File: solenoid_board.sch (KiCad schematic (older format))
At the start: 34 parts, among them J2 MCU_LEFT_LEGS, J3 MCU_RIGHT_LEGS

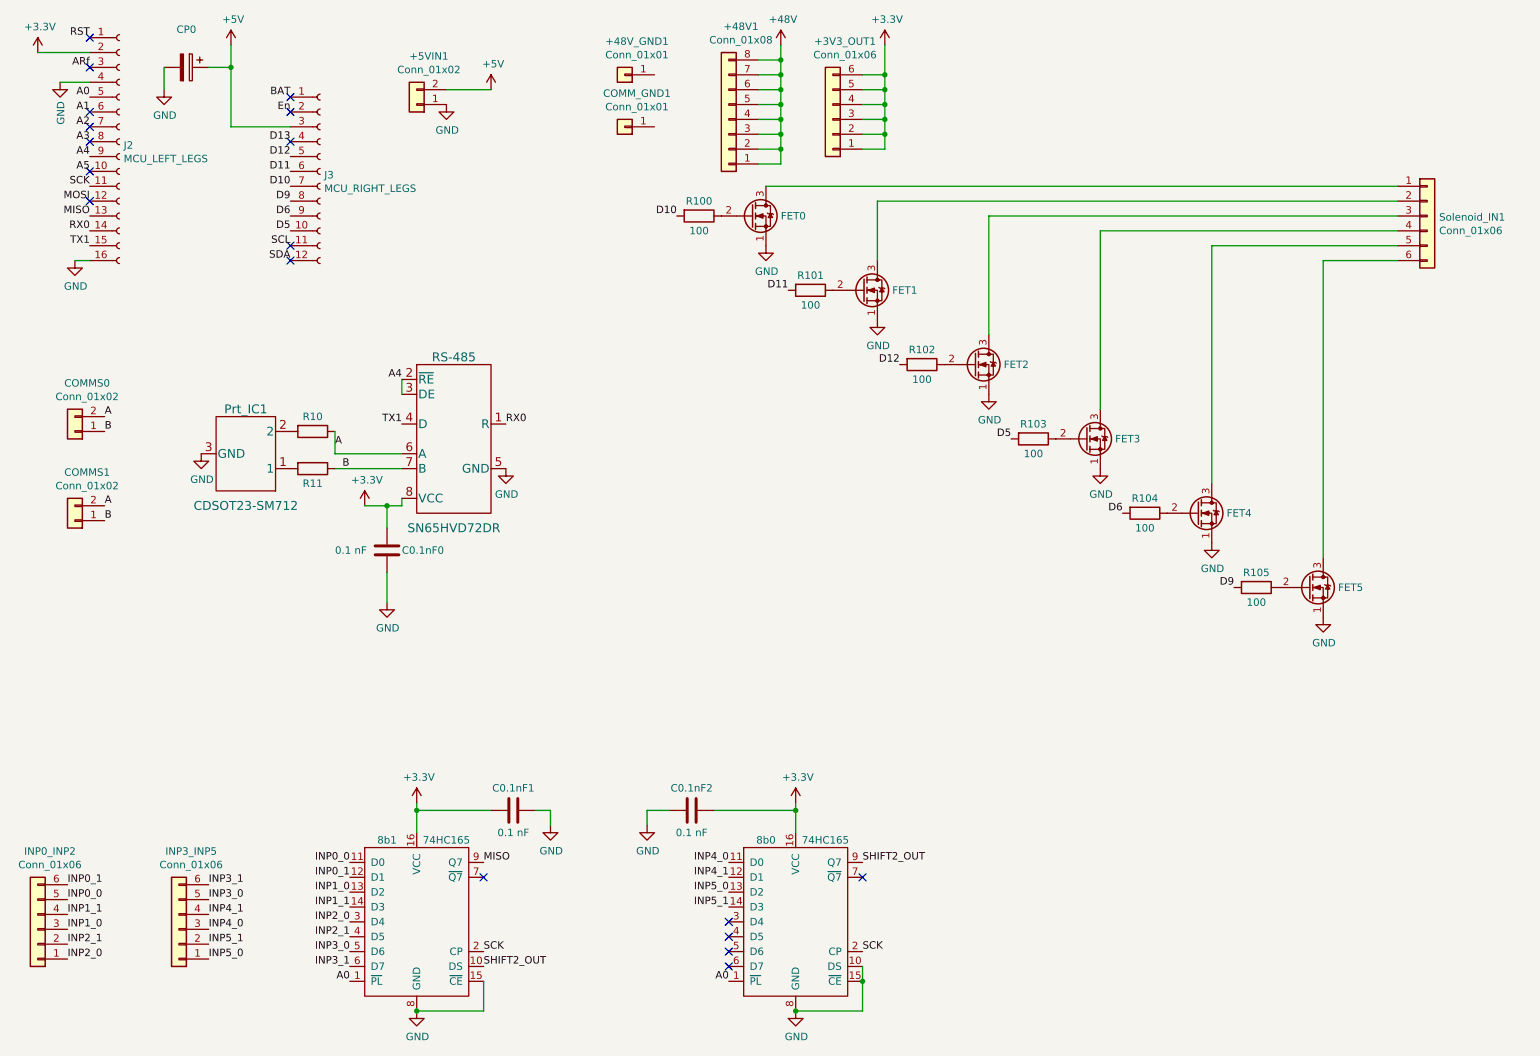
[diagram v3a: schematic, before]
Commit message: Changed pin labels around, re-routed MosFET area, need to route the 8-bit shifter and comms areas.
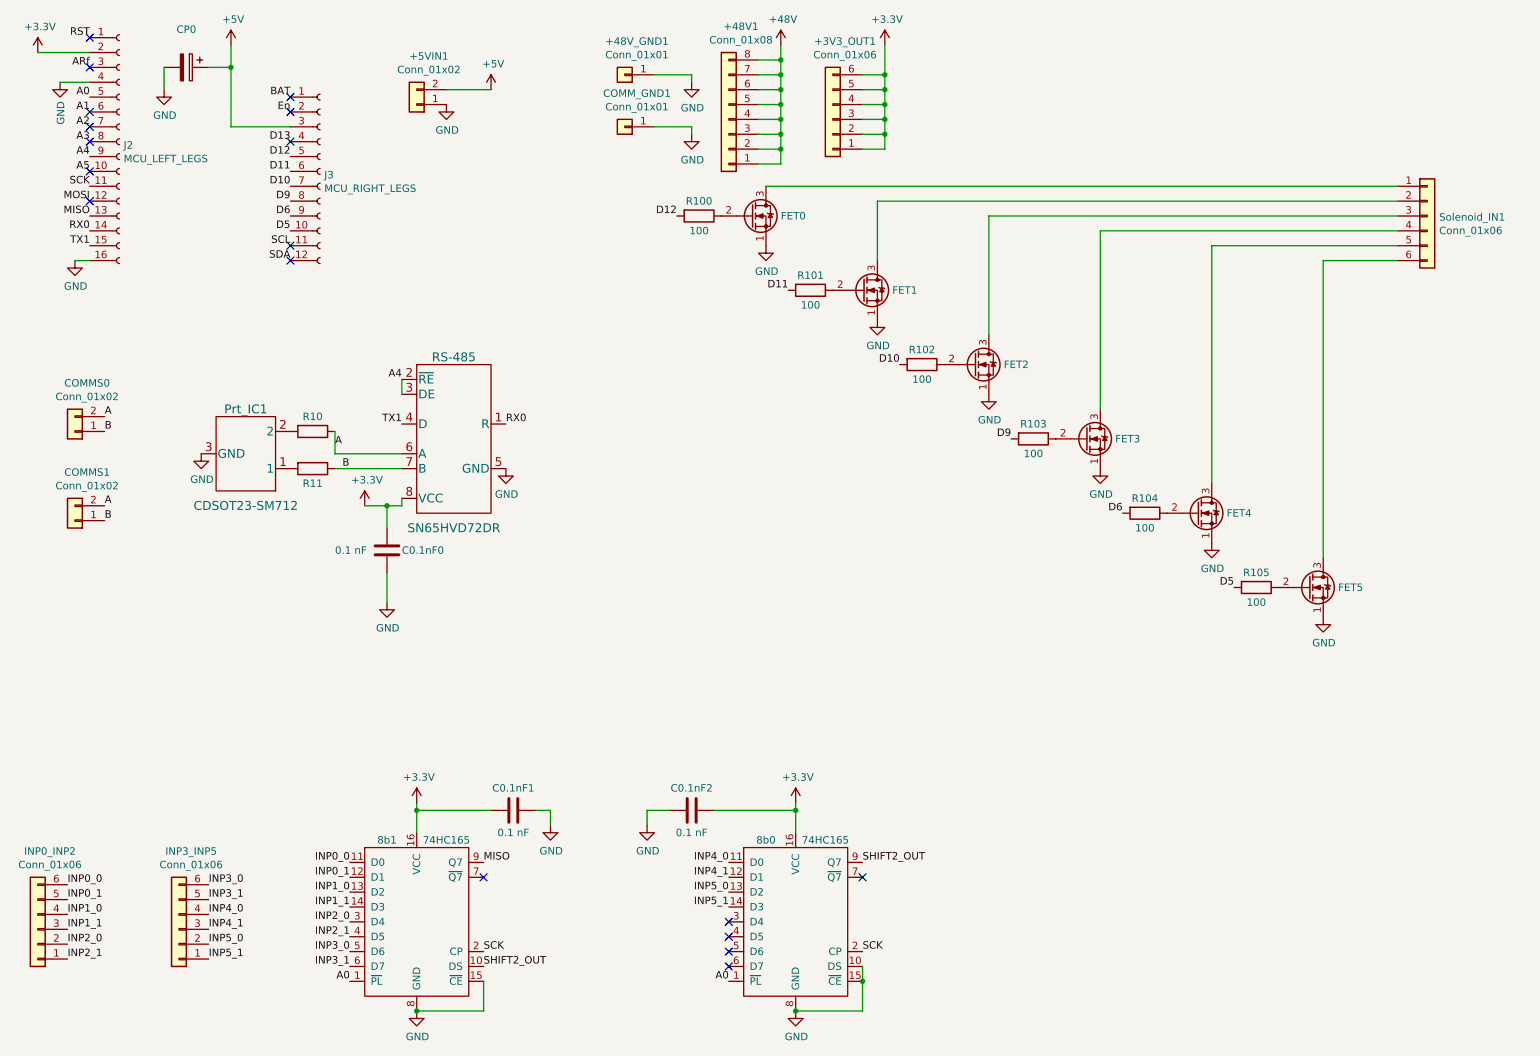
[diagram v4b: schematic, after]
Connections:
- net D10: now also R102.2; no longer R100.2
- net D12: now also R100.2; no longer R102.2
- net D5: now also R105.2; no longer R103.2
- net D9: now also R103.2; no longer R105.2
- net GND: now also +48V_GND1.1 (Pin_1), COMM_GND1.1 (Pin_1)
- net INP0_0: now also INP0_INP2.6 (Pin_6); no longer INP0_INP2.5 (Pin_5)
- net INP0_1: now also INP0_INP2.5 (Pin_5); no longer INP0_INP2.6 (Pin_6)
- net INP1_0: now also INP0_INP2.4 (Pin_4); no longer INP0_INP2.3 (Pin_3)
- net INP1_1: now also INP0_INP2.3 (Pin_3); no longer INP0_INP2.4 (Pin_4)
- net INP2_0: now also INP0_INP2.2 (Pin_2); no longer INP0_INP2.1 (Pin_1)
- net INP2_1: now also INP0_INP2.1 (Pin_1); no longer INP0_INP2.2 (Pin_2)
- net INP3_0: now also INP3_INP5.6 (Pin_6); no longer INP3_INP5.5 (Pin_5)
- net INP3_1: now also INP3_INP5.5 (Pin_5); no longer INP3_INP5.6 (Pin_6)
- net INP4_0: now also INP3_INP5.4 (Pin_4); no longer INP3_INP5.3 (Pin_3)
- net INP4_1: now also INP3_INP5.3 (Pin_3); no longer INP3_INP5.4 (Pin_4)
- net INP5_0: now also INP3_INP5.2 (Pin_2); no longer INP3_INP5.1 (Pin_1)
- net INP5_1: now also INP3_INP5.1 (Pin_1); no longer INP3_INP5.2 (Pin_2)
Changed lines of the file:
@@
 $EndComp
 Text Label 5150 1900 2    50   ~ 0
-D10
+D12
 $Comp
 L MOSFETs:PHP79NQ08LT FET0
@@
 D11
 Text Label 6650 2900 2    50   ~ 0
-D12
+D10
 Text Label 7400 3400 2    50   ~ 0
-D5
+D9
 Text Label 8150 3900 2    50   ~ 0
 D6
 Text Label 8900 4400 2    50   ~ 0
-D9
+D5
+Text Label 1050 6400 0    50   ~ 0
+INP0_0
 Text Label 1050 6500 0    50   ~ 0
-INP0_0
-Text Label 1050 6400 0    50   ~ 0
 INP0_1
+Text Label 1050 6600 0    50   ~ 0
+INP1_0
 Text Label 1050 6700 0    50   ~ 0
-INP1_0
-Text Label 1050 6600 0    50   ~ 0
 INP1_1
+Text Label 1050 6800 0    50   ~ 0
+INP2_0
 Text Label 1050 6900 0    50   ~ 0
-INP2_0
-Text Label 1050 6800 0    50   ~ 0
 INP2_1
+Text Label 2000 6400 0    50   ~ 0
+INP3_0
 Text Label 2000 6500 0    50   ~ 0
-INP3_0
-Text Label 2000 6400 0    50   ~ 0
 INP3_1
+Text Label 2000 6600 0    50   ~ 0
+INP4_0
 Text Label 2000 6700 0    50   ~ 0
-INP4_0
-Text Label 2000 6600 0    50   ~ 0
 INP4_1
+Text Label 2000 6800 0    50   ~ 0
+INP5_0
 Text Label 2000 6900 0    50   ~ 0
-INP5_0
-Text Label 2000 6800 0    50   ~ 0
 INP5_1
 $Comp
@@
 	-1   0    0    1
 $EndComp
+$Comp
+L power:GND #PWR0109
+U 1 1 5E52A503
+P 5250 1350
+F 0 "#PWR0109" H 5250 1100 50  0001 C CNN
+F 1 "GND" H 5255 1177 50  0000 C CNN
+F 2 "" H 5250 1350 50  0001 C CNN
+F 3 "" H 5250 1350 50  0001 C CNN
+	1    5250 1350
+	1    0    0    -1
+$EndComp
+$Comp
+L power:GND #PWR0116
+U 1 1 5E52AD35
+P 5250 1000
+F 0 "#PWR0116" H 5250 750 50  0001 C CNN
+F 1 "GND" H 5255 827 50  0000 C CNN
+F 2 "" H 5250 1000 50  0001 C CNN
+F 3 "" H 5250 1000 50  0001 C CNN
+	1    5250 1000
+	1    0    0    -1
+$EndComp
+Wire Wire Line
+	5250 1000 5250 950
+Wire Wire Line
+	5000 950  5250 950
+Wire Wire Line
+	5250 1350 5250 1300
+Wire Wire Line
+	5250 1300 5000 1300
 $EndSCHEMATC

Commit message: Debugged Solenoid Footprint issue and 3.3V terminal block issue.
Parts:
- FET0, FET1, FET2, FET3, FET4, FET5: footprint Package_TO_SOT_THT:TO-220-3_Vertical -> NXP:PHP79NQ08LT,127
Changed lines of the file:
@@
 F 0 "FET0" H 5850 1900 50  0000 L CNN
 F 1 "PHP79NQ08LT" H 5854 1991 50  0001 L CNN
-F 2 "Package_TO_SOT_THT:TO-220-3_Vertical" H 5850 1825 50  0001 L CIN
+F 2 "NXP:PHP79NQ08LT,127" H 5850 1825 50  0001 L CIN
 F 3 "https://assets.nexperia.com/documents/data-sheet/PHP79NQ08LT.pdf" H 5650 1900 50  0001 L CNN
 F 4 "M" H 5854 1900 50  0001 L CNN "Spice_Primitive"
@@
 F 0 "FET1" H 6600 2400 50  0000 L CNN
 F 1 "PHP79NQ08LT" H 6604 2491 50  0001 L CNN
-F 2 "Package_TO_SOT_THT:TO-220-3_Vertical" H 6600 2325 50  0001 L CIN
+F 2 "NXP:PHP79NQ08LT,127" H 6600 2325 50  0001 L CIN
 F 3 "https://assets.nexperia.com/documents/data-sheet/PHP79NQ08LT.pdf" H 6400 2400 50  0001 L CNN
 F 4 "M" H 6604 2400 50  0001 L CNN "Spice_Primitive"
@@
 F 0 "FET2" H 7350 2900 50  0000 L CNN
 F 1 "PHP79NQ08LT" H 7354 2991 50  0001 L CNN
-F 2 "Package_TO_SOT_THT:TO-220-3_Vertical" H 7350 2825 50  0001 L CIN
+F 2 "NXP:PHP79NQ08LT,127" H 7350 2825 50  0001 L CIN
 F 3 "https://assets.nexperia.com/documents/data-sheet/PHP79NQ08LT.pdf" H 7150 2900 50  0001 L CNN
 F 4 "M" H 7354 2900 50  0001 L CNN "Spice_Primitive"
@@
 F 0 "FET3" H 8100 3400 50  0000 L CNN
 F 1 "PHP79NQ08LT" H 8104 3491 50  0001 L CNN
-F 2 "Package_TO_SOT_THT:TO-220-3_Vertical" H 8100 3325 50  0001 L CIN
+F 2 "NXP:PHP79NQ08LT,127" H 8100 3325 50  0001 L CIN
 F 3 "https://assets.nexperia.com/documents/data-sheet/PHP79NQ08LT.pdf" H 7900 3400 50  0001 L CNN
 F 4 "M" H 8104 3400 50  0001 L CNN "Spice_Primitive"
@@
 F 0 "FET4" H 8850 3900 50  0000 L CNN
 F 1 "PHP79NQ08LT" H 8854 3991 50  0001 L CNN
-F 2 "Package_TO_SOT_THT:TO-220-3_Vertical" H 8850 3825 50  0001 L CIN
+F 2 "NXP:PHP79NQ08LT,127" H 8850 3825 50  0001 L CIN
 F 3 "https://assets.nexperia.com/documents/data-sheet/PHP79NQ08LT.pdf" H 8650 3900 50  0001 L CNN
 F 4 "M" H 8854 3900 50  0001 L CNN "Spice_Primitive"
@@
 F 0 "FET5" H 9600 4400 50  0000 L CNN
 F 1 "PHP79NQ08LT" H 9604 4491 50  0001 L CNN
-F 2 "Package_TO_SOT_THT:TO-220-3_Vertical" H 9600 4325 50  0001 L CIN
+F 2 "NXP:PHP79NQ08LT,127" H 9600 4325 50  0001 L CIN
 F 3 "https://assets.nexperia.com/documents/data-sheet/PHP79NQ08LT.pdf" H 9400 4400 50  0001 L CNN
 F 4 "M" H 9604 4400 50  0001 L CNN "Spice_Primitive"

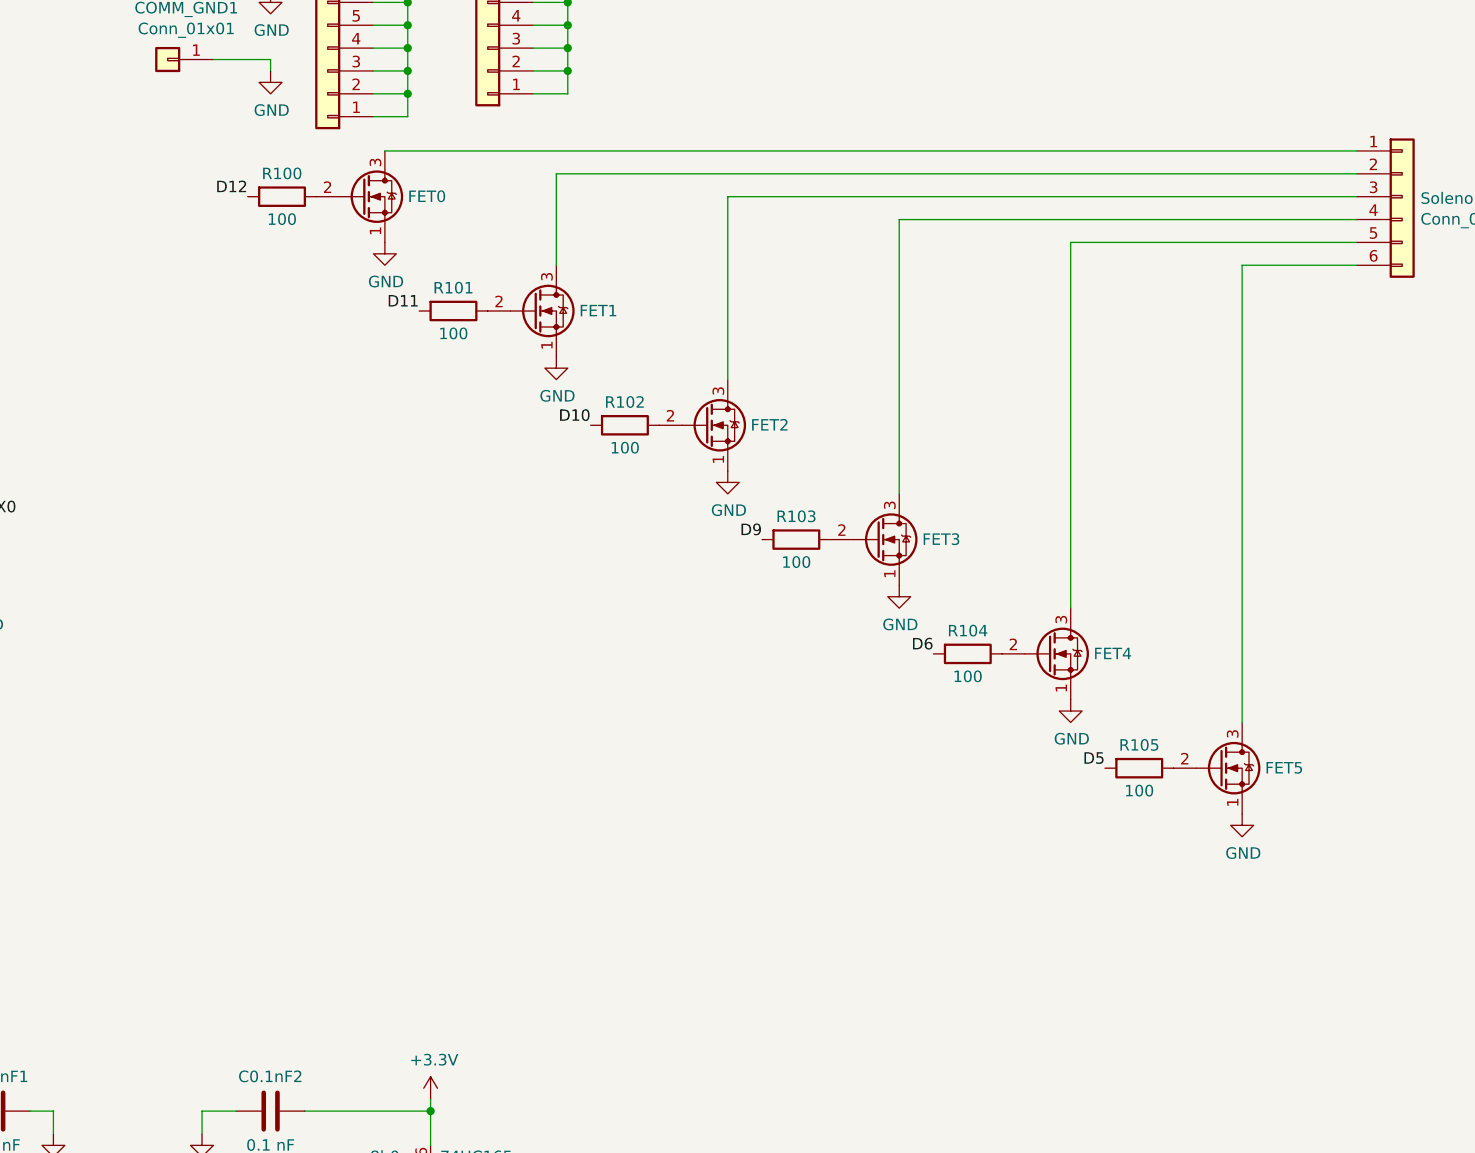
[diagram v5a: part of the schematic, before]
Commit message: added pull up resistor.
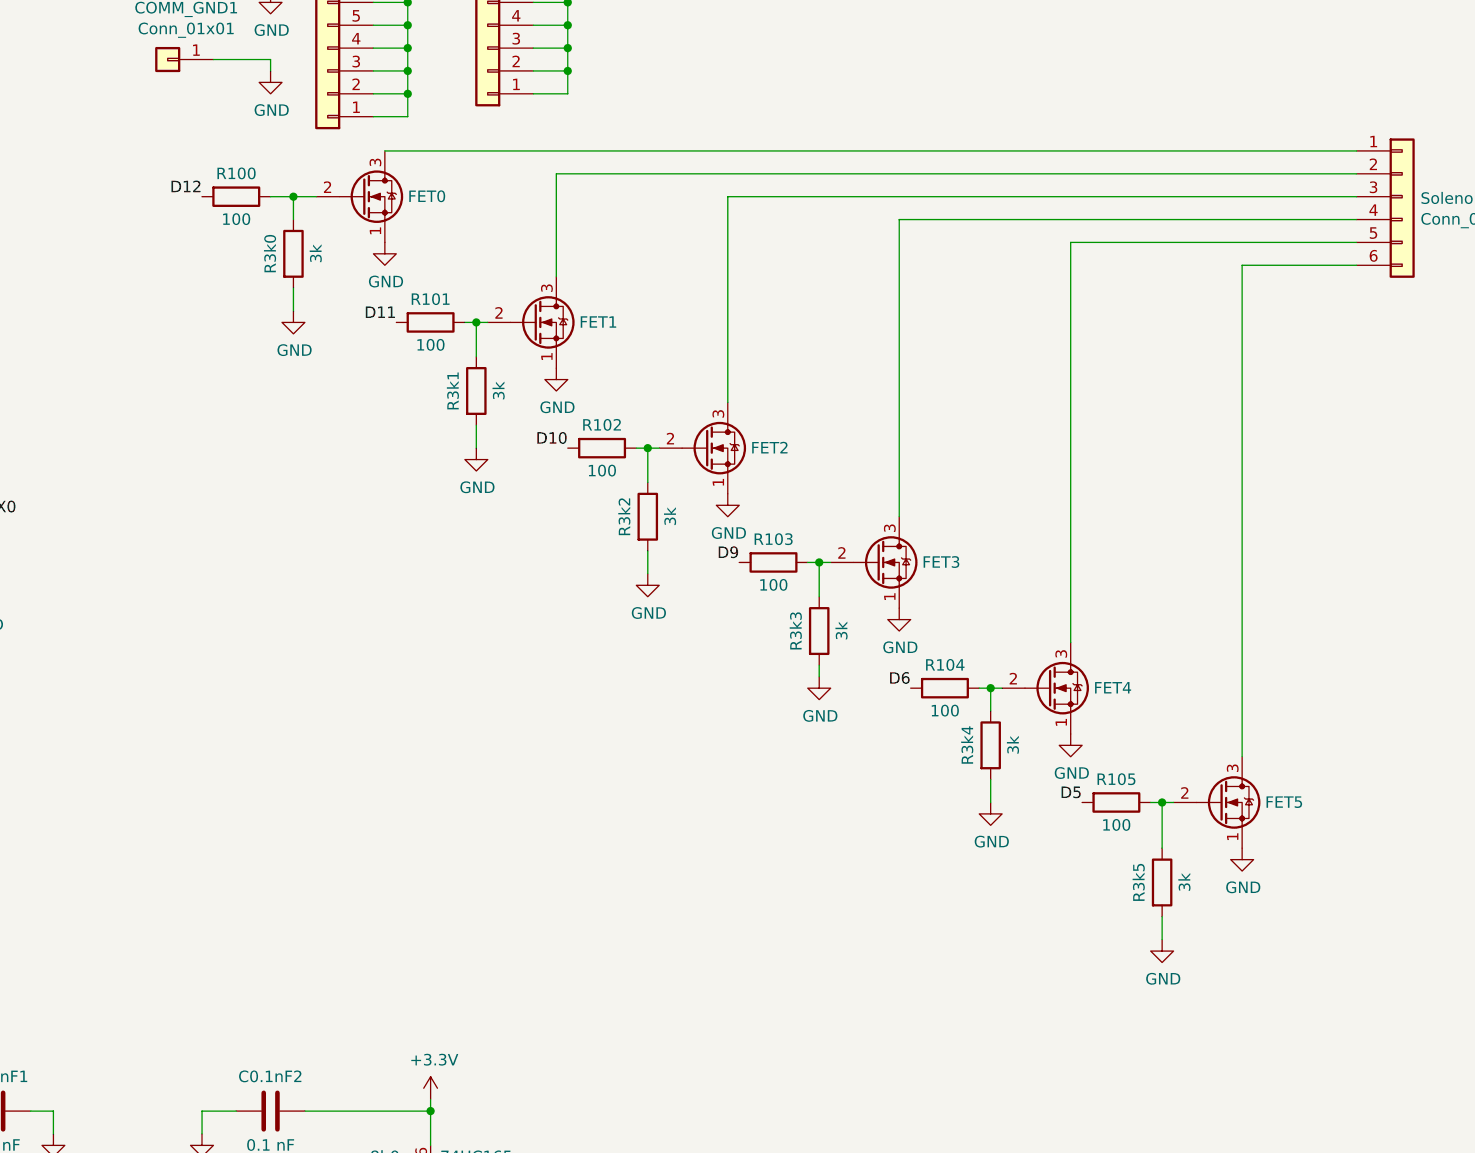
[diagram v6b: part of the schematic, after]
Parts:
- added R3k0, R3k1, R3k2, R3k3, R3k4, R3k5: 3k, Resistor_THT:R_Axial_DIN0204_L3.6mm_D1.6mm_P5.08mm_Vertical, symbol Device:R
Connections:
- net GND: now also R3k0.2, R3k1.2, R3k2.2, R3k3.2, R3k4.2, R3k5.2
- net at FET0.2 (G), R100.1: now also R3k0.1
- net at FET1.2 (G), R101.1: now also R3k1.1
- net at FET2.2 (G), R102.1: now also R3k2.1
- net at FET3.2 (G), R103.1: now also R3k3.1
- net at FET4.2 (G), R104.1: now also R3k4.1
- net at FET5.2 (G), R105.1: now also R3k5.1
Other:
- moved on the sheet: FET1, FET2, FET3, FET4, FET5, R100, R101, R102, R103, R104, R105
